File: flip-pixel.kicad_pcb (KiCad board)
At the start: 2 copper layers, 152.4 x 127 mm, 177 parts, among them Q1 DMN62D0U-7, Q10 STS8DN6LF6AG, Q11 DMN62D0U-7, Q12 DMN62D0U-7, Q13 STS8DN6LF6AG, Q14 DMN62D0U-7, Q15 DMN62D0U-7, Q16 STS8DN6LF6AG, Q17 DMN62D0U-7, Q18 DMN62D0U-7, Q19 STS8DN6LF6AG, Q2 DMN62D0U-7, Q20 DMN62D0U-7, Q21 DMN62D0U-7, Q22 STS8DN6LF6AG, Q23 DMN62D0U-7, Q24 DMN62D0U-7, Q25 STS8DN6LF6AG, Q26 DMN62D0U-7, Q27 DMN62D0U-7, Q28 STS8DN6LF6AG, Q29 DMN62D0U-7, Q3 DMN62D0U-7, Q30 DMN62D0U-7, Q31 STS8DN6LF6AG, Q4 STS8DN6LF6AG, Q5 DMN62D0U-7, Q6 DMN62D0U-7, Q7 STS8DN6LF6AG, Q8 DMN62D0U-7, Q9 DMN62D0U-7, U1 LM2665M6

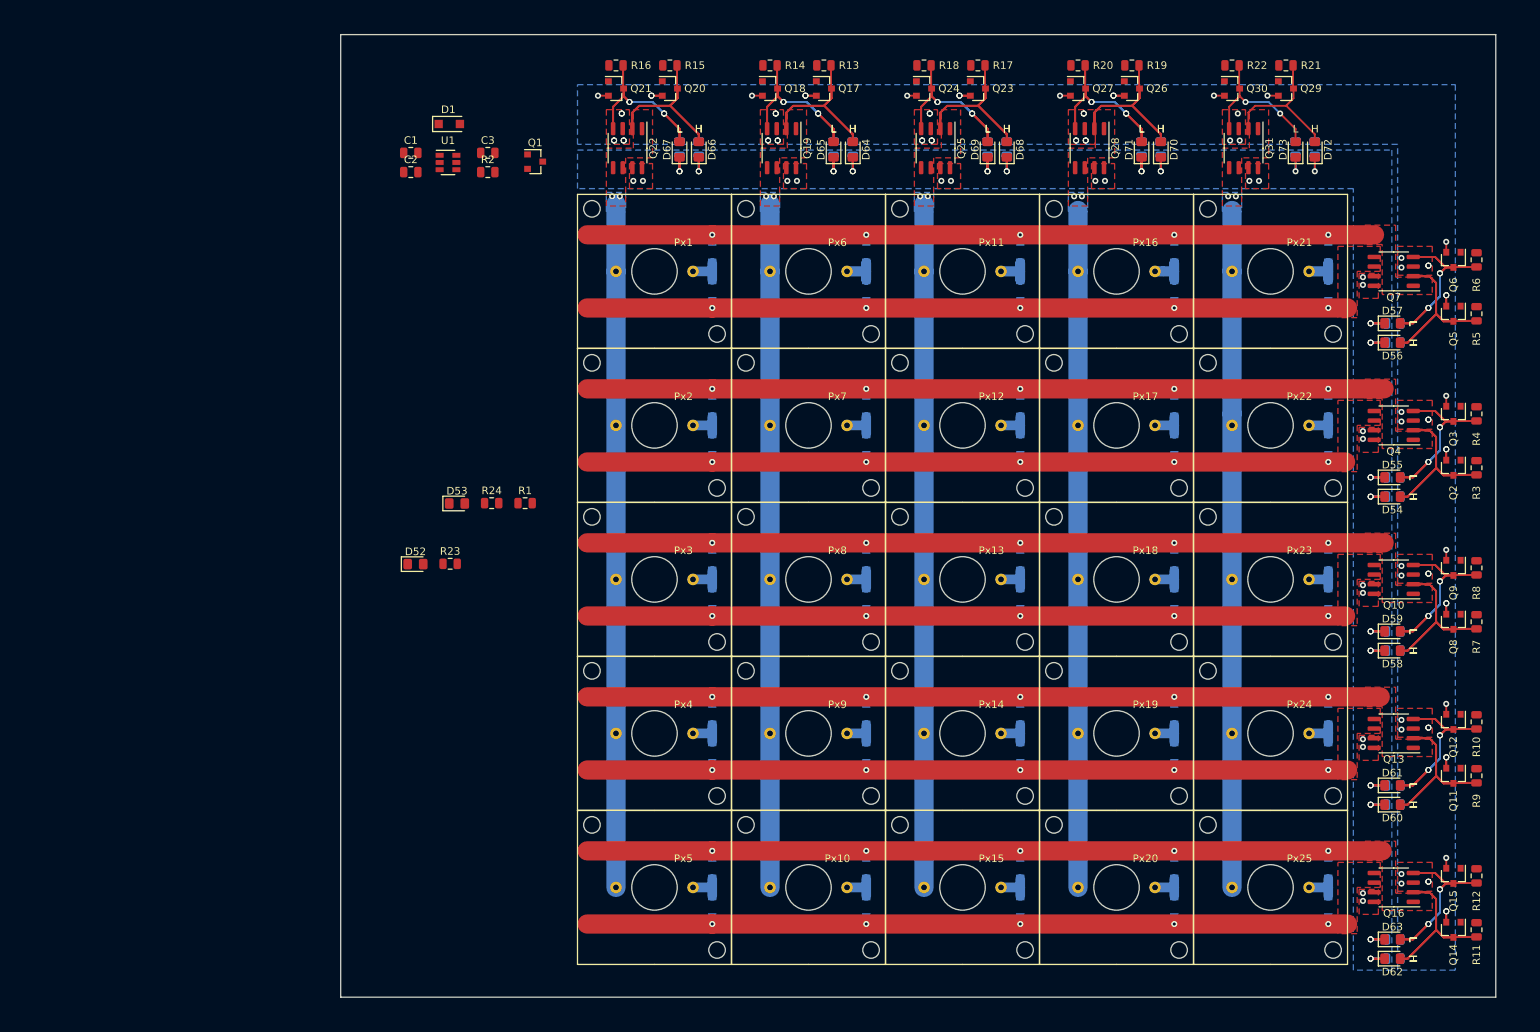
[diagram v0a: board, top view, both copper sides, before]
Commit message: Traces Routed for Charge Pump
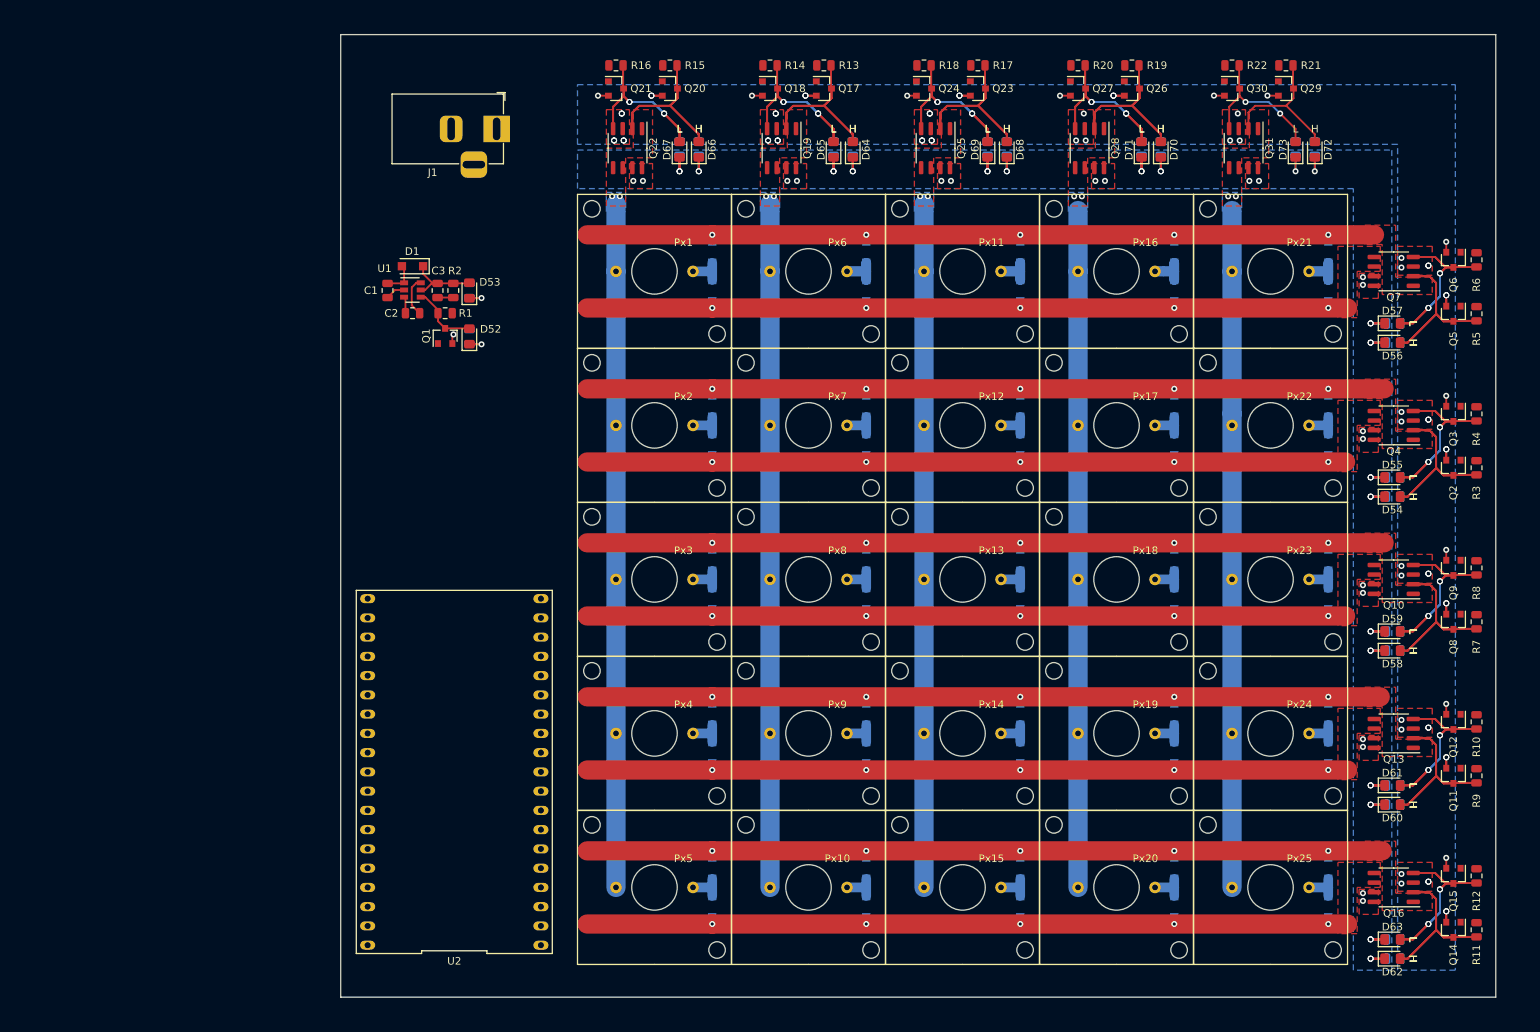
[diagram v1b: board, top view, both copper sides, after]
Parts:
- added J1: Barrel-Jack, Connector_BarrelJack:BarrelJack_Horizontal, F.Cu at (117.1, 40.4)
- added U2: ESP32_DevBoard, Custom-Footprints:DIP-38_900_ELL, F.Cu at (111.5, 125.2)
- R23, R24: moved to B.Cu
- moved D52 30.9 mm to (113.5, 67.8), turned to 90 degrees
- moved R23 30.1 mm to (113.5, 67.8), turned to 90 degrees
- moved R24 28.2 mm to (113.5, 61.7), turned to 90 degrees
- moved D53 28.2 mm to (113.5, 61.7), turned to 90 degrees
- moved R1 27.2 mm to (110.3, 64.7), turned to 180 degrees
- moved Q1 25.9 mm to (110.3, 67.7), turned to 90 degrees
- moved D1 19.4 mm to (106.0, 58.5), turned to 180 degrees
- moved C3 19.3 mm to (109.3, 61.7), turned to 270 degrees
- moved C2 18.6 mm to (106.0, 64.7), turned to 180 degrees
- moved C1 18.4 mm to (102.7, 61.7), turned to 270 degrees
- moved U1 17.5 mm to (106.0, 61.6)
- moved R2 16.3 mm to (111.4, 61.7), turned to 270 degrees
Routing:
- net +10V: track 0.00 -> 10.2 mm
- net /shutdown: track 0.00 -> 9.01 mm
- net GND: track 41.2 -> 47.1 mm, vias 70 -> 74
- net Net-(C2-Pad1): track 0.00 -> 5.27 mm
- net +5V: track 0.00 -> 4.52 mm
- net Net-(D53-Pad1): track 0.00 -> 3.24 mm, vias 0 -> 1
- net Net-(D52-Pad1): track 0.00 -> 3.23 mm, vias 0 -> 1
- net Net-(C2-Pad2): track 0.00 -> 2.19 mm
- net /Column4/Gate_H: vias 6 -> 0

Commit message: Added Current Sensor to Schematic
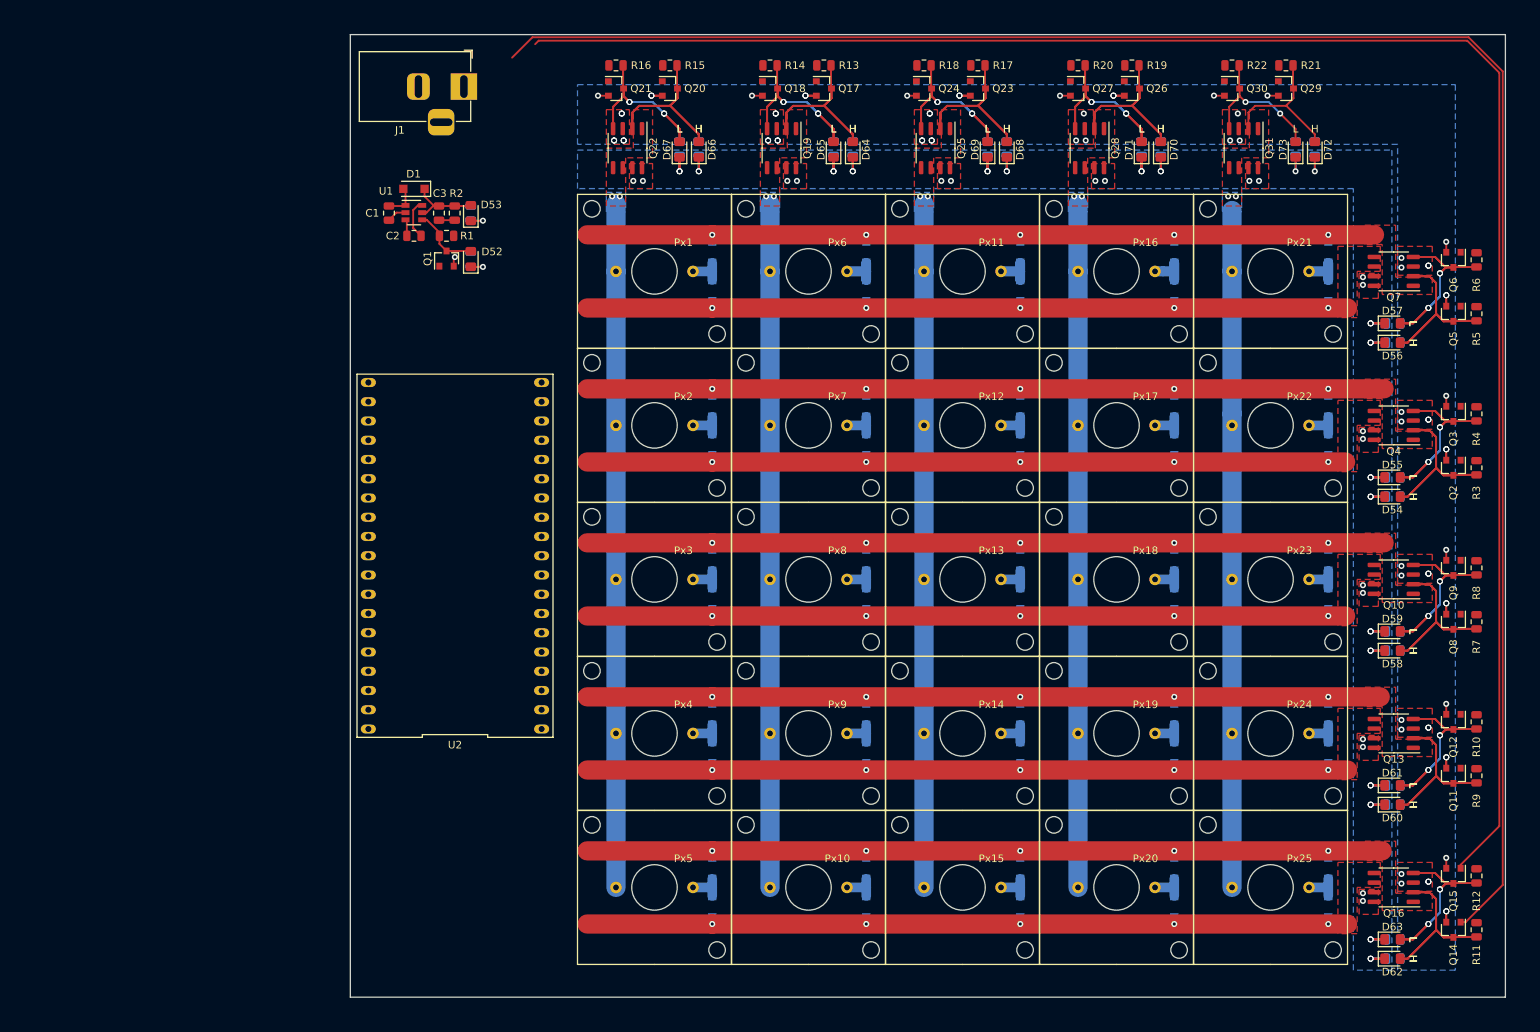
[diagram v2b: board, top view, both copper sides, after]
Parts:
- moved U2 28.5 mm to (111.6, 96.7)
- moved C1 10.2 mm to (102.9, 51.5)
- moved C2 10.2 mm to (106.2, 54.5)
- moved C3 10.2 mm to (109.5, 51.5)
- moved D1 10.2 mm to (106.2, 48.3)
- moved D53 10.2 mm to (113.7, 51.5)
- moved Q1 10.2 mm to (110.5, 57.5)
- moved R1 10.2 mm to (110.5, 54.5)
- moved R2 10.2 mm to (111.6, 51.5)
- moved R24 10.2 mm to (113.7, 51.5)
- moved U1 10.2 mm to (106.2, 51.4)
- moved D52 10.2 mm to (113.7, 57.5)
- moved R23 10.2 mm to (113.7, 57.6)
- moved J1 7.06 mm to (112.8, 34.8)
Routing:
- net /Row5H: track 0.00 -> 248.6 mm
- net /Row5/Low_ct: track 0.00 -> 236.2 mm
- net /PixelMatrix/Col_4: track 89.3 -> 90.2 mm
- added copper zone on B.Cu, net /PixelMatrix/Col_1
- added copper zone on B.Cu, net /PixelMatrix/Col_2

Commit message: starting trace routing
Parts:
- added C4: 0.1uF, Capacitor_SMD:C_0805_2012Metric, F.Cu at (110.0, 40.8)
- added C5: C, Capacitor_SMD:C_0805_2012Metric, F.Cu at (110.0, 43.0)
- added U3: ACS722, Custom-Footprints:SO-8_3.9x4.9mm_P1.27mm, F.Cu at (103.8, 41.8)
- moved U2 13.7 mm to (112.3, 110.4)
- moved J1 4.47 mm to (112.0, 30.4)
- moved D1 2.43 mm to (104.7, 50.2)
- moved C2 2.43 mm to (104.7, 56.4)
- moved C3 2.43 mm to (108.0, 53.4)
- moved D52 2.43 mm to (112.2, 59.5)
- moved D53 2.43 mm to (112.2, 53.4)
- moved Q1 2.43 mm to (109.0, 59.4)
- moved R1 2.43 mm to (109.0, 56.4)
- moved R2 2.43 mm to (110.1, 53.4)
- moved R23 2.43 mm to (112.2, 59.5)
- moved R24 2.43 mm to (112.2, 53.4)
- moved U1 2.43 mm to (104.7, 53.4)
- moved C1 2.43 mm to (101.4, 53.4)
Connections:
- J1 pad 1: +5V -> Net-(J1-Pad1)
- U2 pad 4: Net-(U2-Pad4) -> /current
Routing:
- net +10V: track 10.2 -> 262.9 mm, vias 0 -> 22
- net /Row4H: track 0.00 -> 219.7 mm, vias 0 -> 1
- net /Row4/Low_ct: track 0.00 -> 210.9 mm, vias 0 -> 1
- net /Col5H: track 0.00 -> 197.9 mm
- net /Row3H: track 0.00 -> 196.1 mm, vias 0 -> 1
- net /Row3/Low_ct: track 0.00 -> 187.3 mm, vias 0 -> 1
- net /Column5/Low_ct: track 0.00 -> 187.0 mm
- net /Row2H: track 0.00 -> 172.5 mm, vias 0 -> 1
- net /Col4H: track 0.00 -> 170.2 mm
- net /Row2/Low_ct: track 0.00 -> 163.8 mm, vias 0 -> 1
- net /Column4/Low_ct: track 0.00 -> 159.4 mm
- net /Row1H: track 0.00 -> 148.9 mm, vias 0 -> 1
- net /Col3H: track 0.00 -> 142.4 mm
- net /Row1/Low_ct: track 0.00 -> 140.1 mm, vias 0 -> 1
- net /Column3/Low_ct: track 0.00 -> 131.5 mm
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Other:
- board size 152.4 x 127 mm -> 154.9 x 129.5 mm

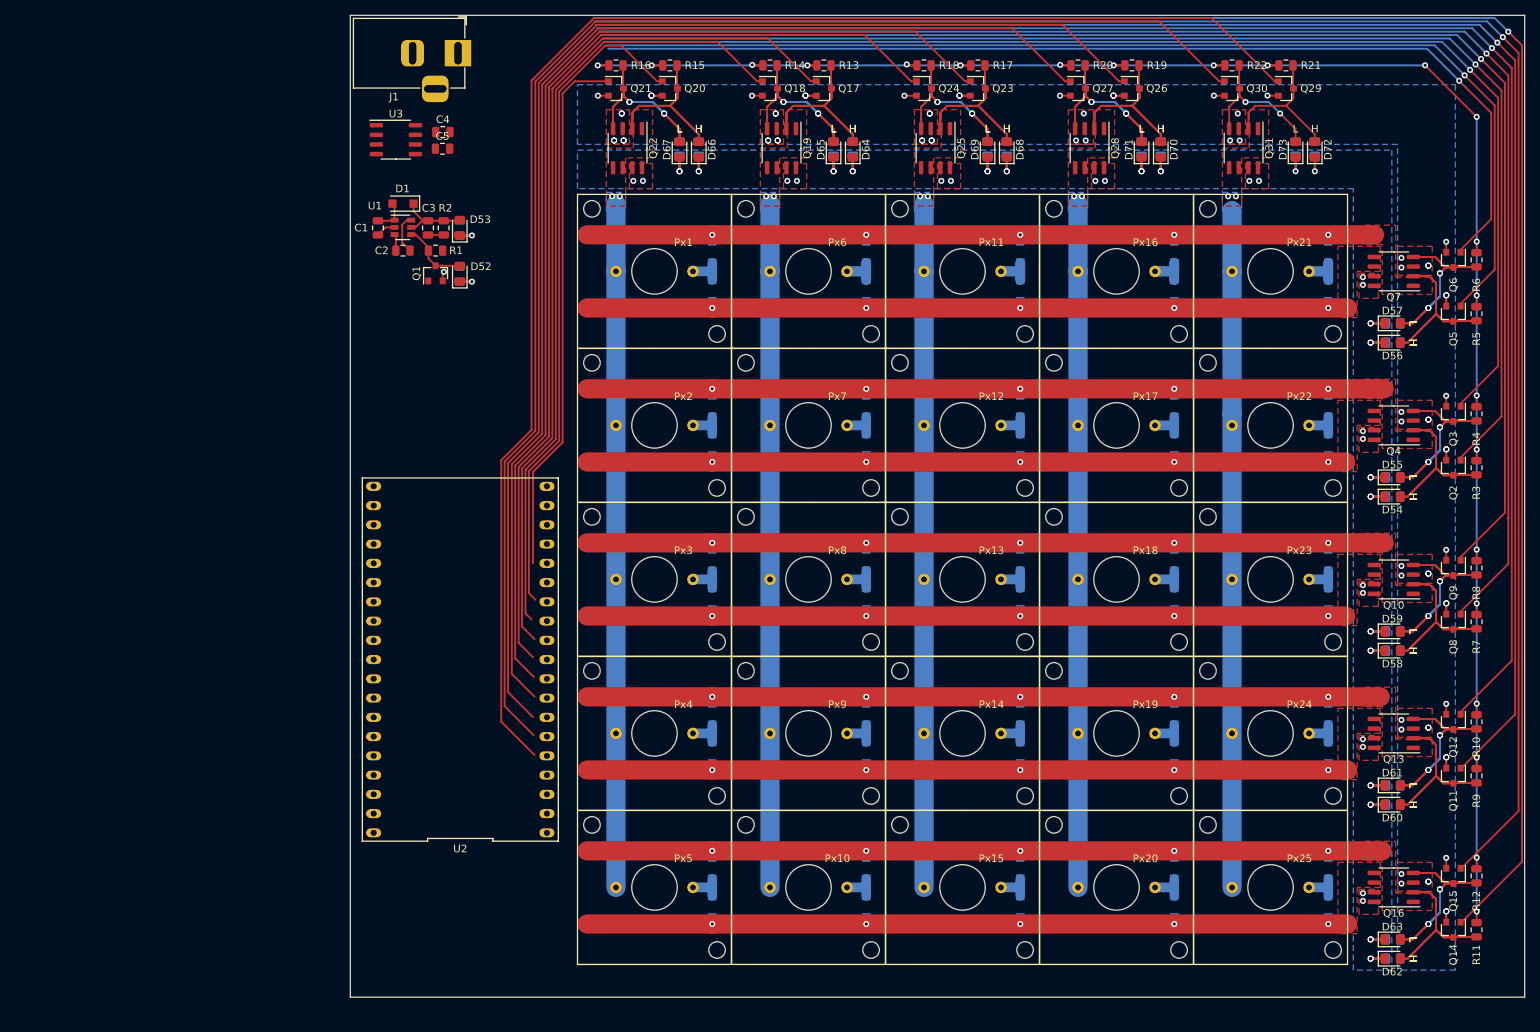
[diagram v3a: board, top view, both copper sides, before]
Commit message: Routed from drivers to controller
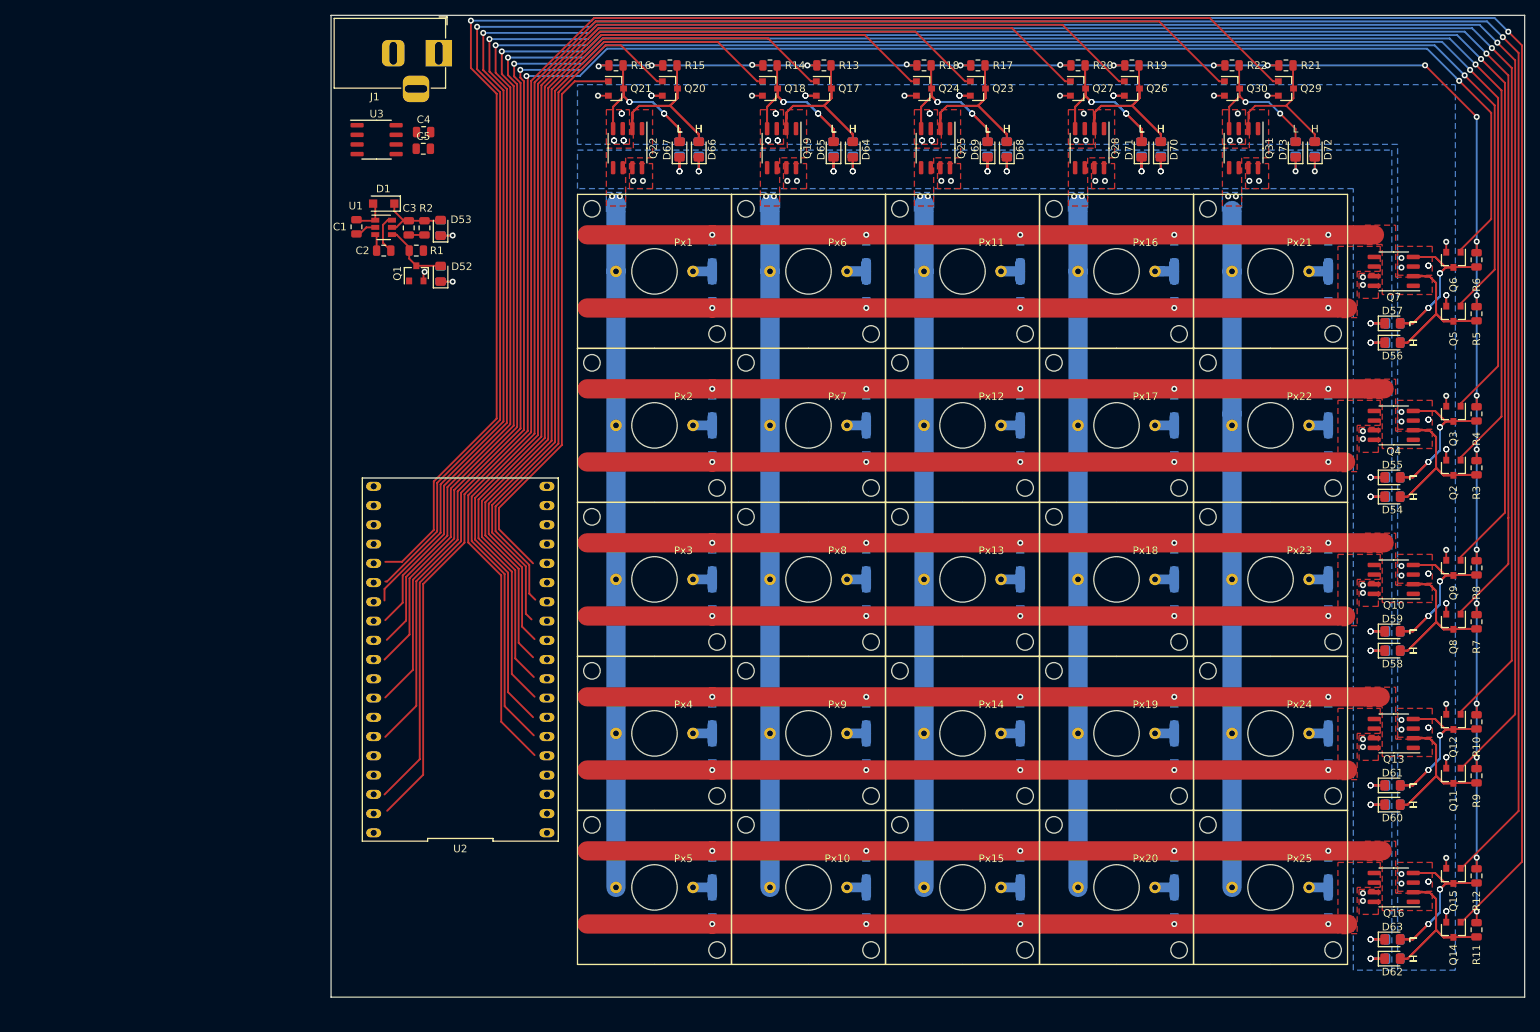
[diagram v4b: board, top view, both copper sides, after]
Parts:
- moved C1 2.84 mm to (98.6, 53.3)
- moved C2 2.54 mm to (102.2, 56.4)
- moved C3 2.54 mm to (105.5, 53.4)
- moved C4 2.54 mm to (107.5, 40.8)
- moved D1 2.54 mm to (102.2, 50.2)
- moved D52 2.54 mm to (109.7, 59.5)
- moved D53 2.54 mm to (109.7, 53.4)
- moved J1 2.54 mm to (109.5, 30.4)
- moved Q1 2.54 mm to (106.5, 59.4)
- moved R1 2.54 mm to (106.5, 56.4)
- moved R2 2.54 mm to (107.6, 53.4)
- moved R23 2.54 mm to (109.7, 59.5)
- moved R24 2.54 mm to (109.7, 53.4)
- moved C5 2.54 mm to (107.4, 43.0)
- moved U1 2.54 mm to (102.2, 53.4)
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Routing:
- net /Row1/Low_ct: track 140.1 -> 257.0 mm, vias 1 -> 2
- net /Row1H: track 148.9 -> 265.0 mm, vias 1 -> 2
- net /Row2/Low_ct: track 163.8 -> 273.4 mm, vias 1 -> 2
- net /Row2H: track 172.5 -> 278.1 mm, vias 1 -> 2
- net /Row3/Low_ct: track 187.3 -> 289.3 mm, vias 1 -> 2
- net /Row3H: track 196.1 -> 296.5 mm, vias 1 -> 2
- net /Row4/Low_ct: track 210.9 -> 310.0 mm, vias 1 -> 2
- net /Row4H: track 219.7 -> 317.4 mm, vias 1 -> 2
- net /Row5/Low_ct: track 234.5 -> 331.1 mm, vias 1 -> 2
- net /Row5H: track 243.1 -> 339.6 mm, vias 1 -> 2
- net /Column1/Low_ct: track 70.3 -> 74.0 mm
- net /Col1H: track 87.1 -> 90.8 mm
- net /Col2H: track 114.9 -> 118.5 mm
- net /Column3/Low_ct: track 131.5 -> 135.2 mm
- net /Col3H: track 142.4 -> 146.0 mm
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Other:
- board size 154.9 x 129.5 mm -> 157.5 x 129.5 mm
